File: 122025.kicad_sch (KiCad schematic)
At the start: 42 parts, among them Q1 2N5088, Q2 2N4401, SW1 SW_SPST, U1 JRC4558

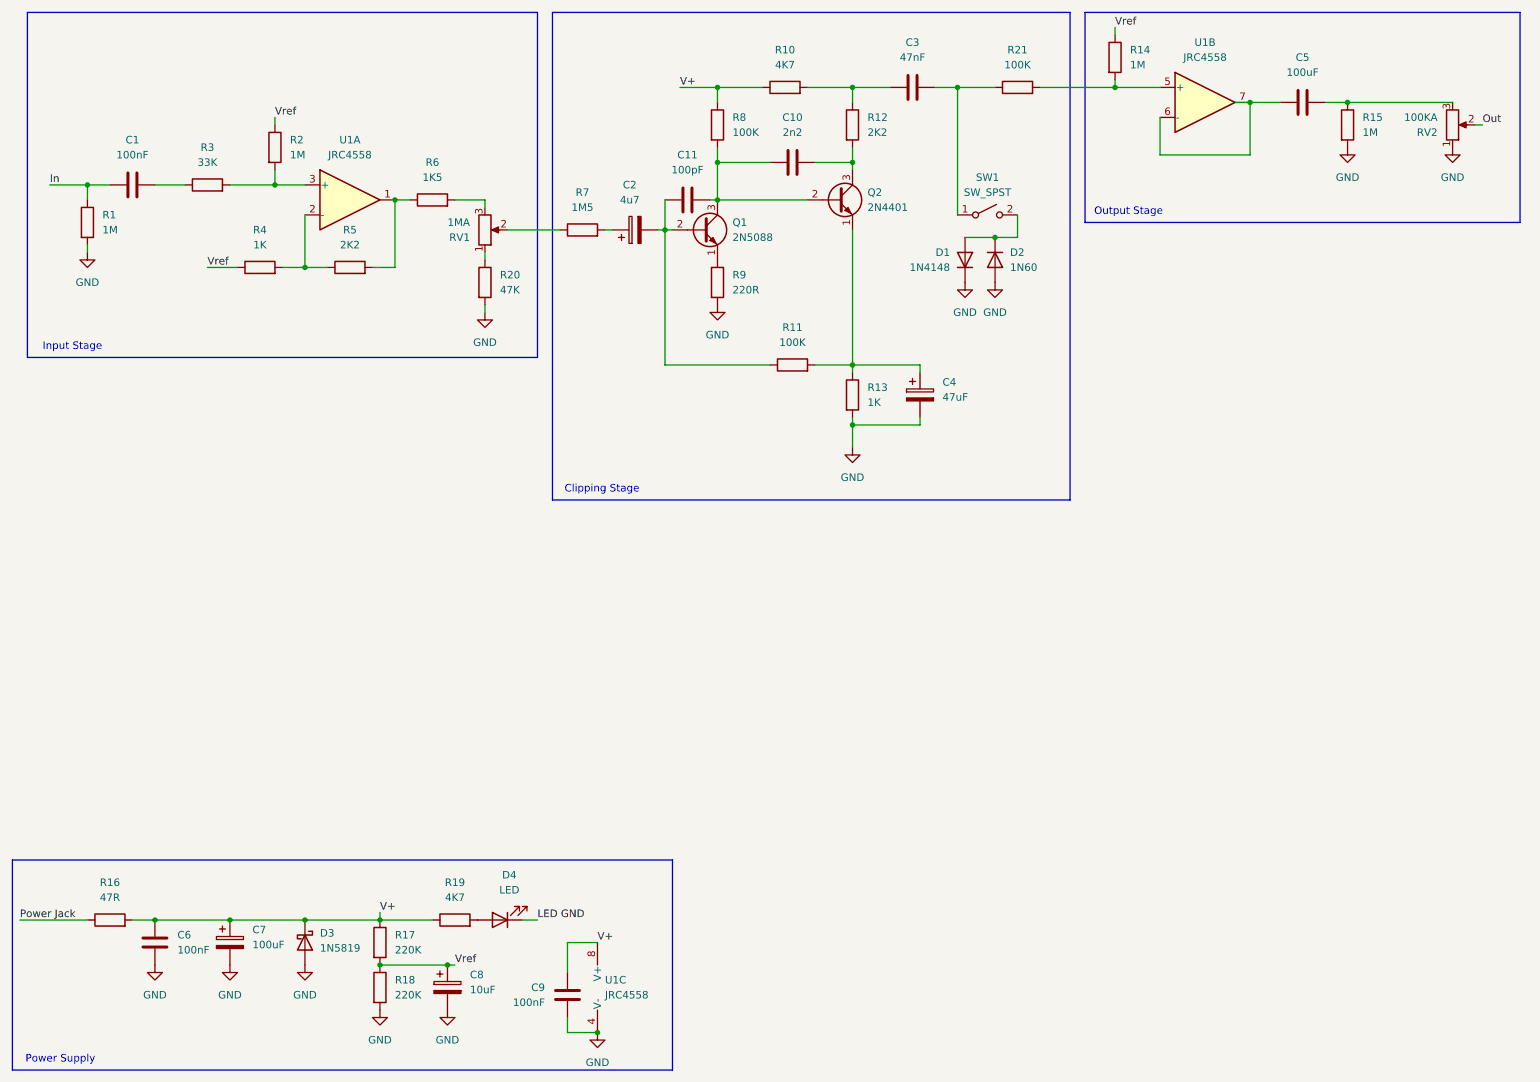
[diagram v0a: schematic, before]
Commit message: Added tone and propper gain control
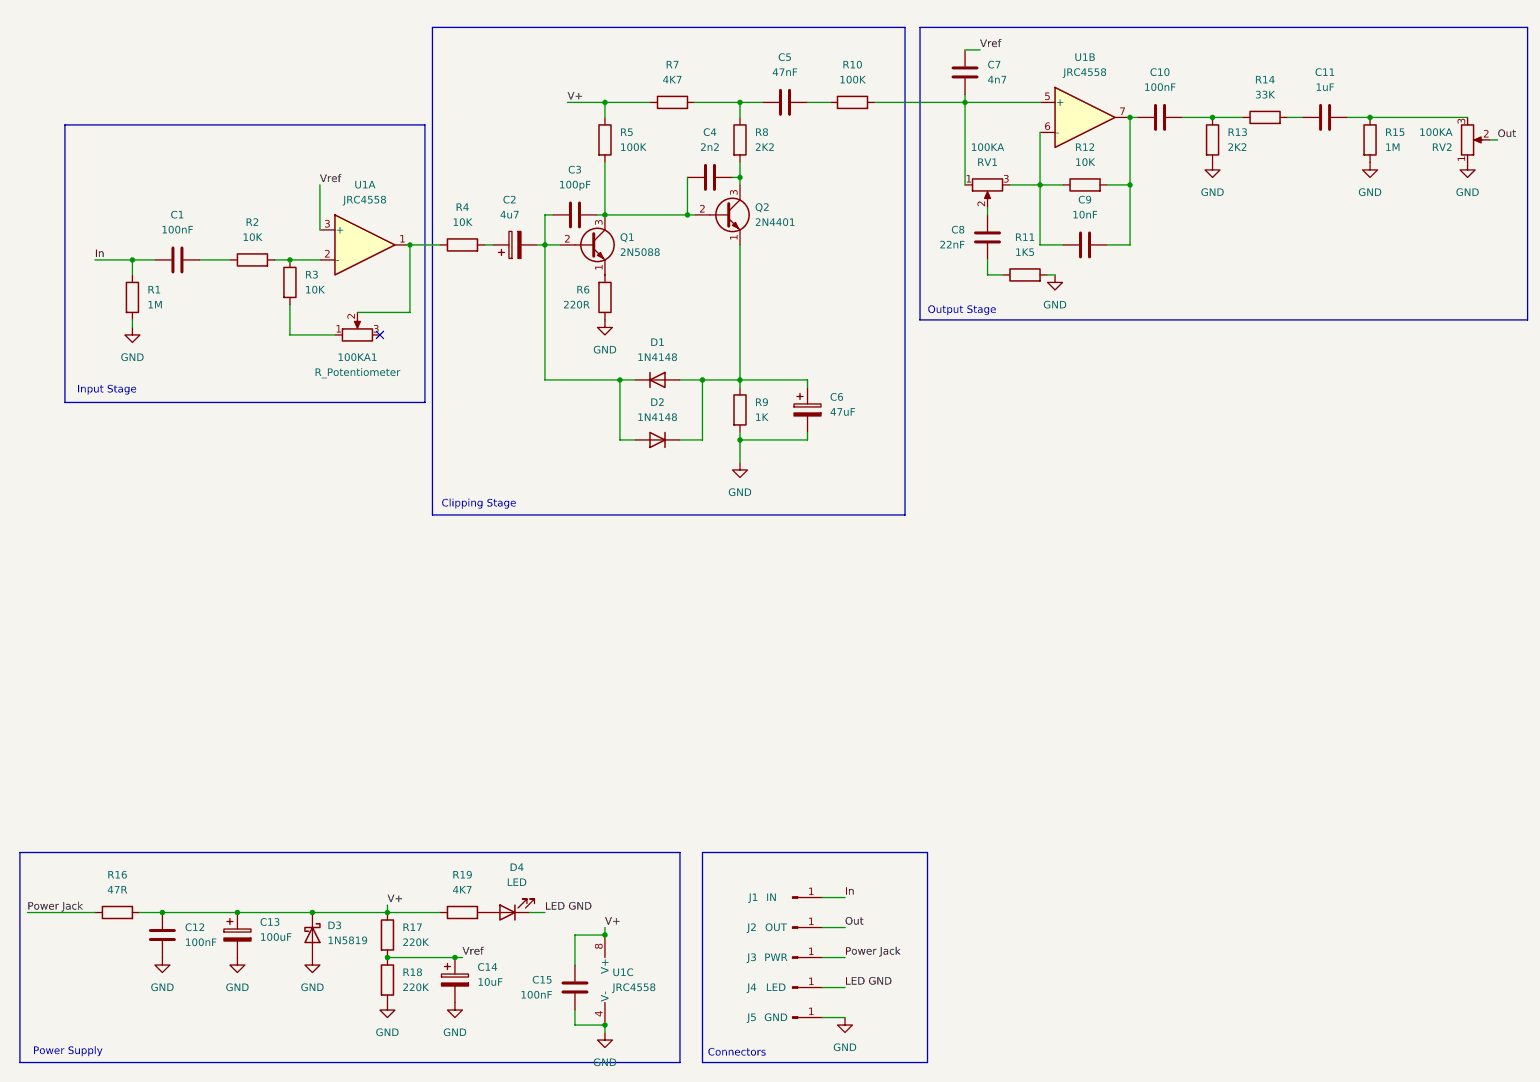
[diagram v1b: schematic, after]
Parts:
- removed R2: 1M, symbol Device:R
- removed R20: 47K, symbol Device:R
- removed R4: 1K, symbol Device:R
- removed R5: 2K2, symbol Device:R
- removed R6: 1K5, symbol Device:R
- removed SW1: SW_SPST, symbol Switch:SW_SPST
- added 100KA1: R_Potentiometer, symbol Device:R_Potentiometer
- added C10: 100nF, symbol Device:C
- added C7: 4n7, symbol Device:C
- added C8: 22nF, symbol Device:C
- added C9: 10nF, symbol Device:C
- added J1: IN, Connector_PinHeader_2.00mm:PinHeader_1x01_P2.00mm_Vertical, symbol Connector:Conn_01x01_Pin
- added J2: OUT, Connector_PinHeader_2.00mm:PinHeader_1x01_P2.00mm_Vertical, symbol Connector:Conn_01x01_Pin
- added J3: PWR, Connector_PinHeader_2.00mm:PinHeader_1x01_P2.00mm_Vertical, symbol Connector:Conn_01x01_Pin
- added J4: LED, Connector_PinHeader_2.00mm:PinHeader_1x01_P2.00mm_Vertical, symbol Connector:Conn_01x01_Pin
- added J5: GND, Connector_PinHeader_2.00mm:PinHeader_1x01_P2.00mm_Vertical, symbol Connector:Conn_01x01_Pin
- added R12, R3: 10K, symbol Device:R
- added R13: 2K2, symbol Device:R
- C11: renamed from C5; value 100uF -> 1uF
- D2: value 1N60 -> 1N4148
- R11: value 100K -> 1K5
- R14: value 1M -> 33K
- R2: renamed from R3; value 33K -> 10K
- R4: renamed from R7; value 1M5 -> 10K
- RV1: value 1MA -> 100KA; footprint Potentiometer_THT:Potentiometer_Alpha_RD901F-40-00D_Single_Vertical -> (none)
- renumbered C6 to C12, C7 to C13, C8 to C14, C9 to C15, C11 to C3, C10 to C4, C3 to C5, C4 to C6, R21 to R10, R8 to R5, R9 to R6, R10 to R7, R12 to R8, R13 to R9
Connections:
- net GND: now also R11.2, R6.1, J5.1 (Pin_1), R13.2; no longer D1.1 (K), D2.2 (A), R6.2
- net In: now also J1.1 (Pin_1)
- net LED GND: now also J4.1 (Pin_1)
- net Out: now also J2.1 (Pin_1)
- net Power Jack: now also J3.1 (Pin_1)
- net Vref: now also U1.3 (+), C7.1; no longer R14.1
- net at R10.2, U1.5 (+): now also RV1.1, C7.2; no longer R14.2
- net at C2.2, C3.1, Q1.2 (B): now also D1.1 (K), D2.2 (A); no longer R11.1
- net at D1.2 (A), D2.1 (K): now also C6.1, Q2.1 (E), R9.1
- net at Q1.1 (E): now also R6.2; no longer R6.1
- net at R4.1: now also U1.1, 100KA1.2; no longer RV1.2
- net at RV1.3: now also U1.6 (-), C9.1, R12.1
- net at U1.2 (-): now also R2.2, R3.1
- new net: C10.2, R13.1, R14.1
- new net: 100KA1.1, R3.2
- new net: C8.2, RV1.2
- new net: C10.1, C9.2, R12.2, U1.7
- new net: C11.1, R14.2
- new net: C8.1, R11.1
- no-connect marks 0 -> 1
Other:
- note added: "Connectors"
- title: Guitar Distortion/Fuzz Pedal -> Guitar Fuzz Pedal
- moved on the sheet: C1, C11, C12, C13, C14, C15, C2, C3, C4, C5, C6, D3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
